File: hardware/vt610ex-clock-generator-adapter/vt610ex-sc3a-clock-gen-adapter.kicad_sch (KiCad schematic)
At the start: 10 parts, among them J11 Conn_01x01_Pin, J12 Conn_01x01_Pin, J21 Conn_01x01_Pin, J22 Conn_01x01_Pin, J30 Conn_01x03_Pin

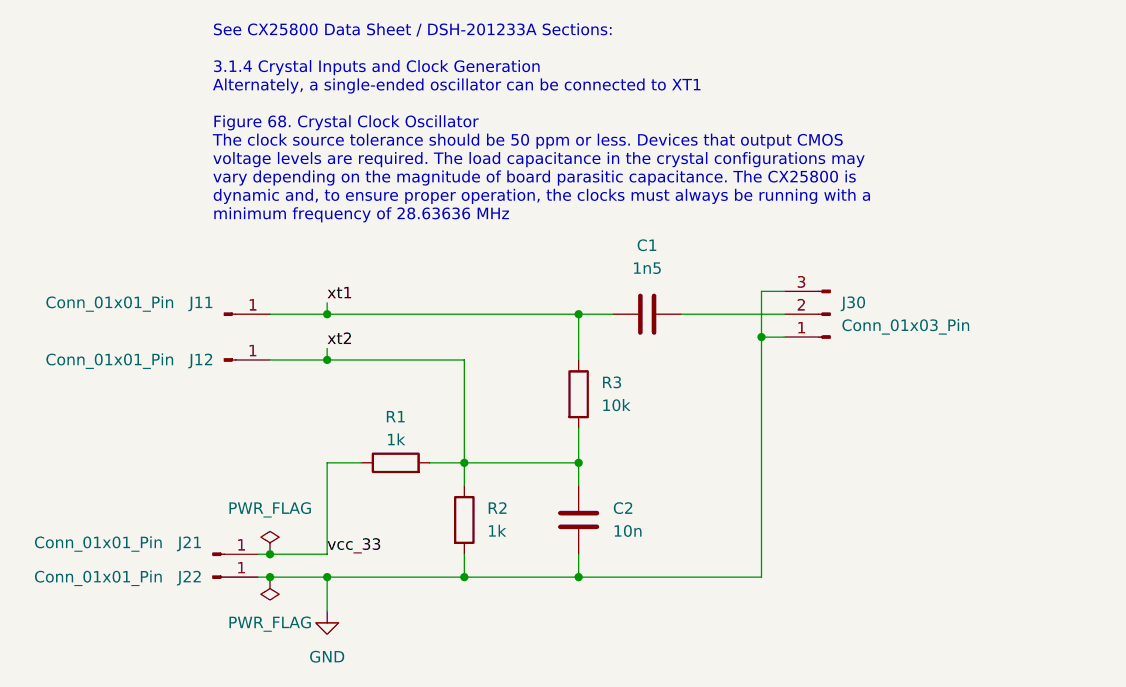
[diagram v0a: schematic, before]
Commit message: Resolve "Extend build guide to explain SMA connectors for clock lines"
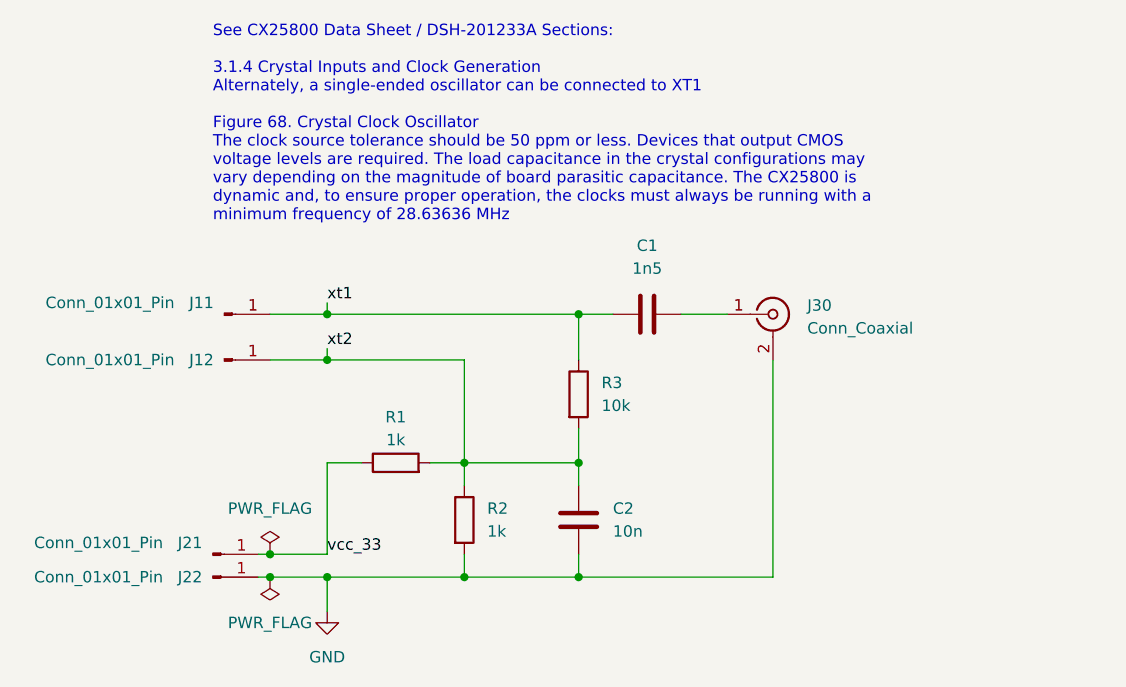
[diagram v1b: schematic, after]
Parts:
- removed J30: Conn_01x03_Pin, custom-vt610ex-sc3a:PinHeader_1x03_P2.54mm_Edge, symbol Connector:Conn_01x03_Pin
- added J30: Conn_Coaxial, Connector_Coaxial:SMA_Samtec_SMA-J-P-X-ST-EM1_EdgeMount, symbol Connector:Conn_Coaxial
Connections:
- net GND: now also J30.2 (Ext)
- net at C1.1: now also J30.1 (In)
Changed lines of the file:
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@@
   (title_block
     (title "${proj-title}")
-    (date "2023-09-10")
+    (date "2023-11-26")
     (rev "${proj-version}")
     (company "${proj-author}")
@@
   (junction (at 114.3 121.92) (diameter 0) (color 0 0 0 0)
   )
-  (junction (at 162.56 95.25) (diameter 0) (color 0 0 0 0)
-  )
   (junction (at 114.3 97.79) (diameter 0) (color 0 0 0 0)
   )
@@
     (stroke (width 0) (type default))
   )
-  (wire (pts (xy 162.56 121.92) (xy 162.56 95.25))
-    (stroke (width 0) (type default))
-  )
   (wire (pts (xy 142.24 111.76) (xy 142.24 109.22))
     (stroke (width 0) (type default))
@@
     (stroke (width 0) (type default))
   )
-  (wire (pts (xy 153.67 92.71) (xy 165.1 92.71))
+  (wire (pts (xy 163.83 121.92) (xy 163.83 97.79))
     (stroke (width 0) (type default))
   )
@@
     (stroke (width 0) (type default))
   )
-  (wire (pts (xy 162.56 90.17) (xy 165.1 90.17))
-    (stroke (width 0) (type default))
-  )
   (wire (pts (xy 114.3 92.71) (xy 142.24 92.71))
     (stroke (width 0) (type default))
@@
     (stroke (width 0) (type default))
   )
-  (wire (pts (xy 162.56 95.25) (xy 162.56 90.17))
-    (stroke (width 0) (type default))
-  )
   (wire (pts (xy 114.3 109.22) (xy 118.11 109.22))
     (stroke (width 0) (type default))
@@
     (stroke (width 0) (type default))
   )
-  (wire (pts (xy 142.24 121.92) (xy 162.56 121.92))
-    (stroke (width 0) (type default))
-  )
-  (wire (pts (xy 162.56 95.25) (xy 165.1 95.25))
+  (wire (pts (xy 142.24 121.92) (xy 163.83 121.92))
     (stroke (width 0) (type default))
   )
   (wire (pts (xy 142.24 109.22) (xy 129.54 109.22))
+    (stroke (width 0) (type default))
+  )
+  (wire (pts (xy 153.67 92.71) (xy 158.75 92.71))
     (stroke (width 0) (type default))
   )
@@
         (path "/1dbcd153-f5a7-436e-9c59-1246c5e4537f"
           (reference "#FLG01") (unit 1)
-        )
-      )
-    )
-  )
-  (symbol (lib_id "Connector:Conn_01x03_Pin") (at 170.18 92.71 180) (unit 1)
-    (in_bom yes) (on_board yes) (dnp no) (fields_autoplaced)
-    (property "Reference" "J30" (at 171.45 91.44 0)
-      (effects (font (size 1.27 1.27)) (justify right))
-    )
-    (property "Value" "Conn_01x03_Pin" (at 171.45 93.98 0)
-      (effects (font (size 1.27 1.27)) (justify right))
-    )
-    (property "Footprint" "custom-vt610ex-sc3a:PinHeader_1x03_P2.54mm_Edge" (at 170.18 92.71 0)
-      (effects (font (size 1.27 1.27)) hide)
-    )
-    (property "Datasheet" "~" (at 170.18 92.71 0)
-      (effects (font (size 1.27 1.27)) hide)
-    )
-    (pin "1")
-    (pin "2")
-    (pin "3")
-    (instances
-      (project "vt610ex-sc3a-clock-gen-adapter"
-        (path "/1dbcd153-f5a7-436e-9c59-1246c5e4537f"
-          (reference "J30") (unit 1)
         )
       )
@@
         )
       )
+    )
+  )
+  (symbol (lib_id "Connector:Conn_Coaxial") (at 163.83 92.71 0) (unit 1)
+    (in_bom yes) (on_board yes) (dnp no) (fields_autoplaced)
+    (property "Reference" "J30" (at 167.64 91.7332 0)
+      (effects (font (size 1.27 1.27)) (justify left))
+    )
+    (property "Value" "Conn_Coaxial" (at 167.64 94.2732 0)
+      (effects (font (size 1.27 1.27)) (justify left))
+    )
+    (property "Footprint" "Connector_Coaxial:SMA_Samtec_SMA-J-P-X-ST-EM1_EdgeMount" (at 163.83 92.71 0)
+      (effects (font (size 1.27 1.27)) hide)
+    )
+    (property "Datasheet" " ~" (at 163.83 92.71 0)
+      (effects (font (size 1.27 1.27)) hide)
+    )
+    (pin "1")
+    (pin "2")
+    (instances
+      (project "vt610ex-sc3a-clock-gen-adapter"
+        (path "/1dbcd153-f5a7-436e-9c59-1246c5e4537f"
+          (reference "J30") (unit 1)
+        )
+      )
